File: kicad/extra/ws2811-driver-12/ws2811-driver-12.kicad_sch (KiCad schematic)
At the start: 12 parts, among them J1 Conn_01x13_Pin, J3 RJ45 IN, J4 RJ45 OUT, U1 WS2811, U2 WS2811, U3 WS2811, U4 WS2811

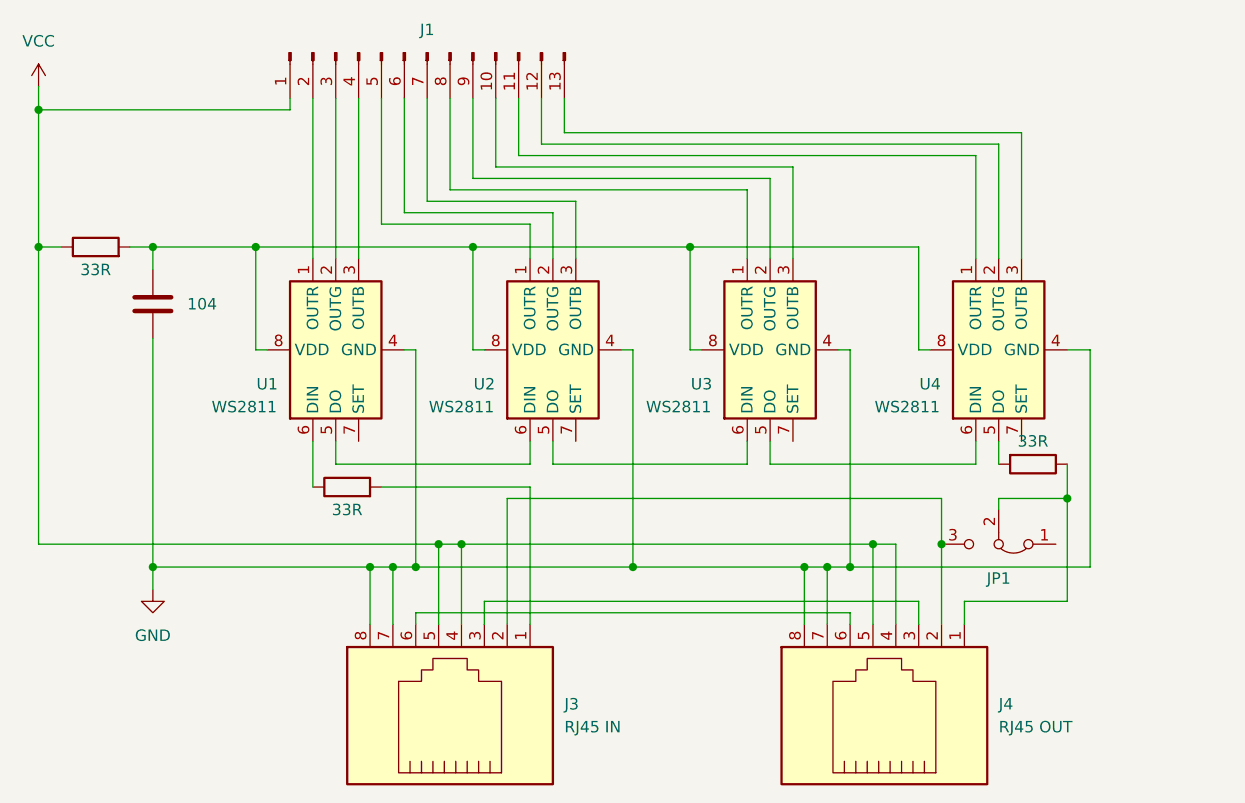
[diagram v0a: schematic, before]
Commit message: feat: Rework WS2811 boards (Rev 2.0)
* Change RJ45 pinout: The data signal is always paired with a ground
  line to increase signal stability, and the changed wireing eases the
  traces on the boards.

* All WS2811 driver boards have a three pin header for direct drive now.
  They can be directly connected to a signal decoder, e.g. for testing.

* The adapter boards has jumper pins to bypass RJ45 jacks, in case you
  want to connect another board using the final pin header.

* Change pin header component to a better available JCSC parts number.

* Move RJ45 jacks on driver boards a bit more off the board, so that
  there is less space between the jack and the outer side of the Watti
  carrier. This makes it easier to plug in and out RJ45 cables as
  the latches are easier to reach.

Fixes #4
Fixes #5
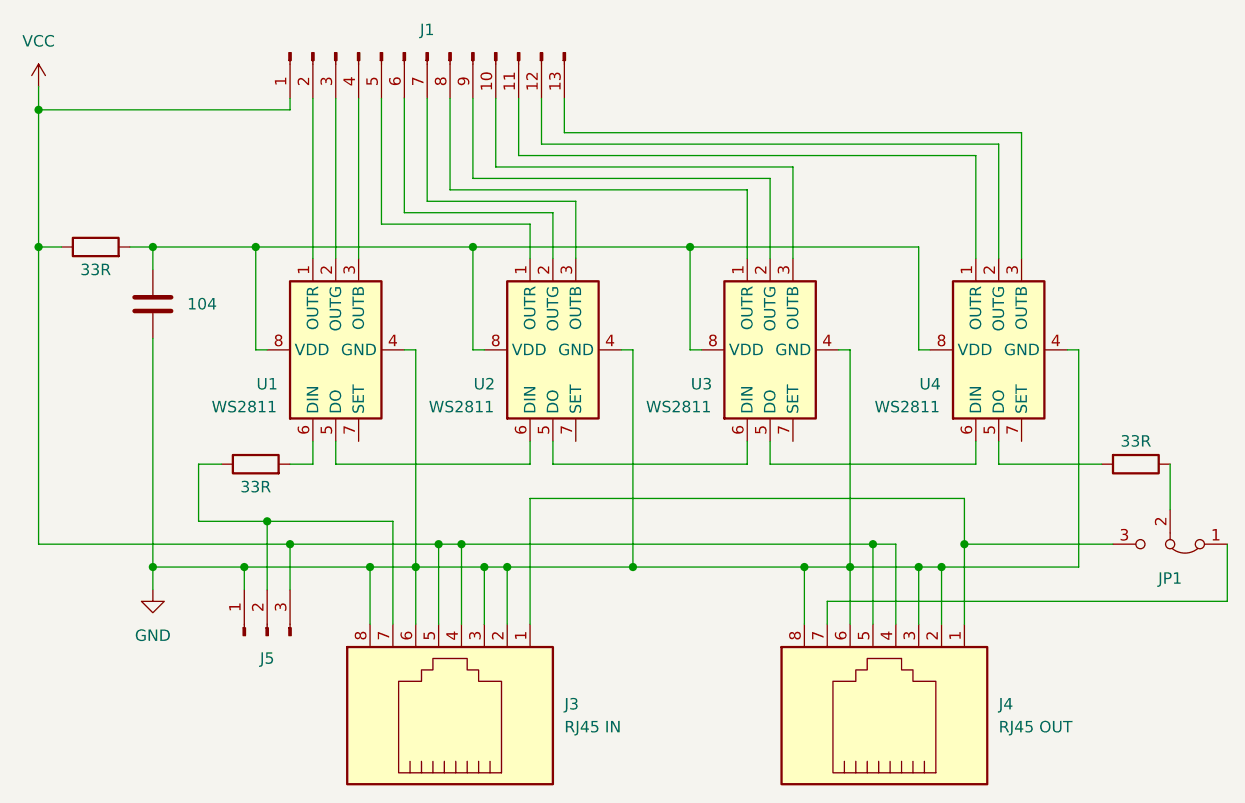
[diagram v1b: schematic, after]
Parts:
- added J5: Conn_01x03_Pin, Connector_PinHeader_2.54mm:PinHeader_1x03_P2.54mm_Vertical, symbol Connector:Conn_01x03_Pin
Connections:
- net GND: now also J3.2, J3.3, J3.6, J4.2, J4.3, J4.6, J5.1 (Pin_1); no longer J3.7, J4.7
- net VCC: now also J5.3 (Pin_3)
- net at JP1.2 (C), R3.1: no longer J4.1
- net at J3.1: now also J4.1, JP1.3 (B); no longer R2.2
- net at R2.1: now also J3.7, J5.2 (Pin_2); no longer U1.6 (DIN)
- net at JP1.1 (A): now also J4.7
- new net: R2.2, U1.6 (DIN)
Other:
- moved on the sheet: JP1
